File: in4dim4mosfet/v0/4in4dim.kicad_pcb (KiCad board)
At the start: 2 copper layers, 100.1 x 86.4 mm, 89 parts, among them IC1 ATTINY48-A, J1 RJ45, J2 RJ45, J3 CONN_6, K1 CONN_3, P1 CONN_5, P100 CONN_2, P101 CONN_2, P102 CONN_2, P103 CONN_2, P105 CONN_2, P106 CONN_2, P110 CONN_2, P120 CONN_2, P130 CONN_2, P140 CONN_2, P2 CONN_2, P3 CONN_6X2, Q1 SPP20N60C3, Q2 SPP20N60C3, Q3 SPP20N60C3, Q4 SPP20N60C3, U1 7805, U2 LTV847, U3 LTV847

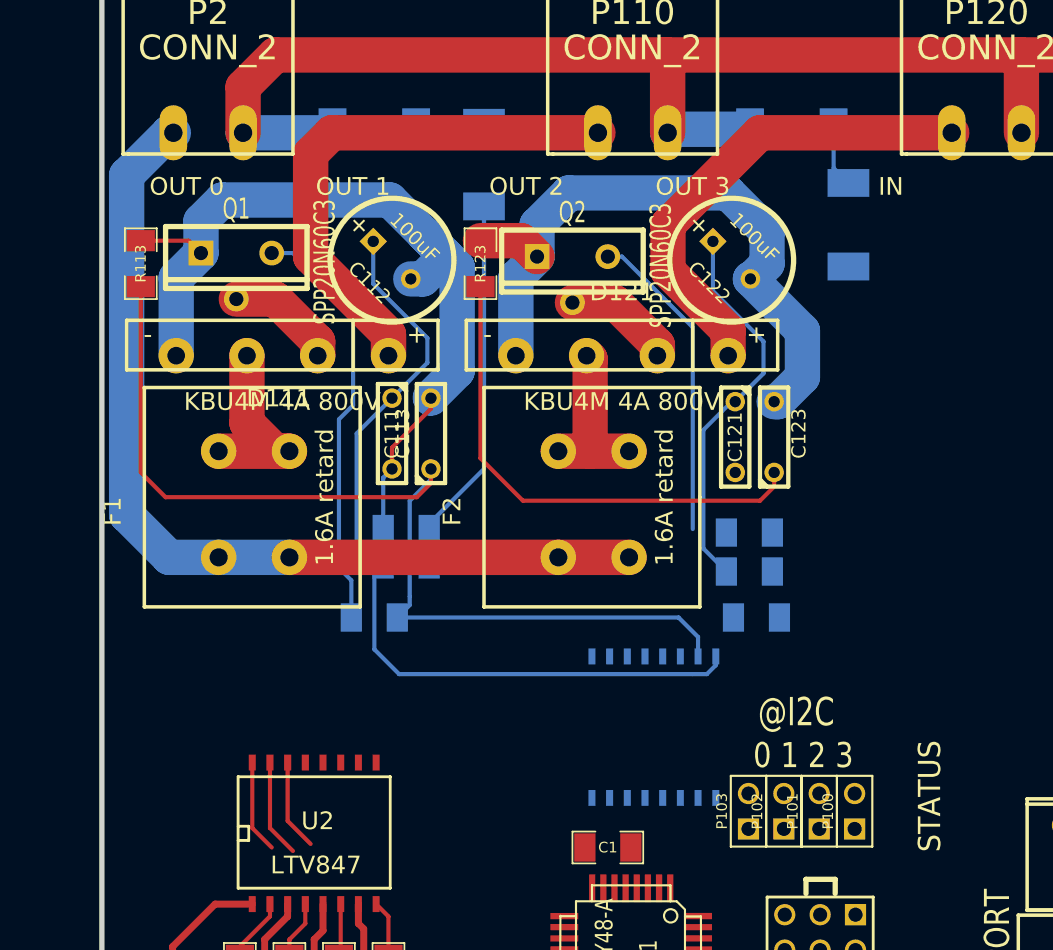
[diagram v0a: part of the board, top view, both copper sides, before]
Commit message: amelioration routage partie puissance pour liberer les deux faces pour le passage de la puissance
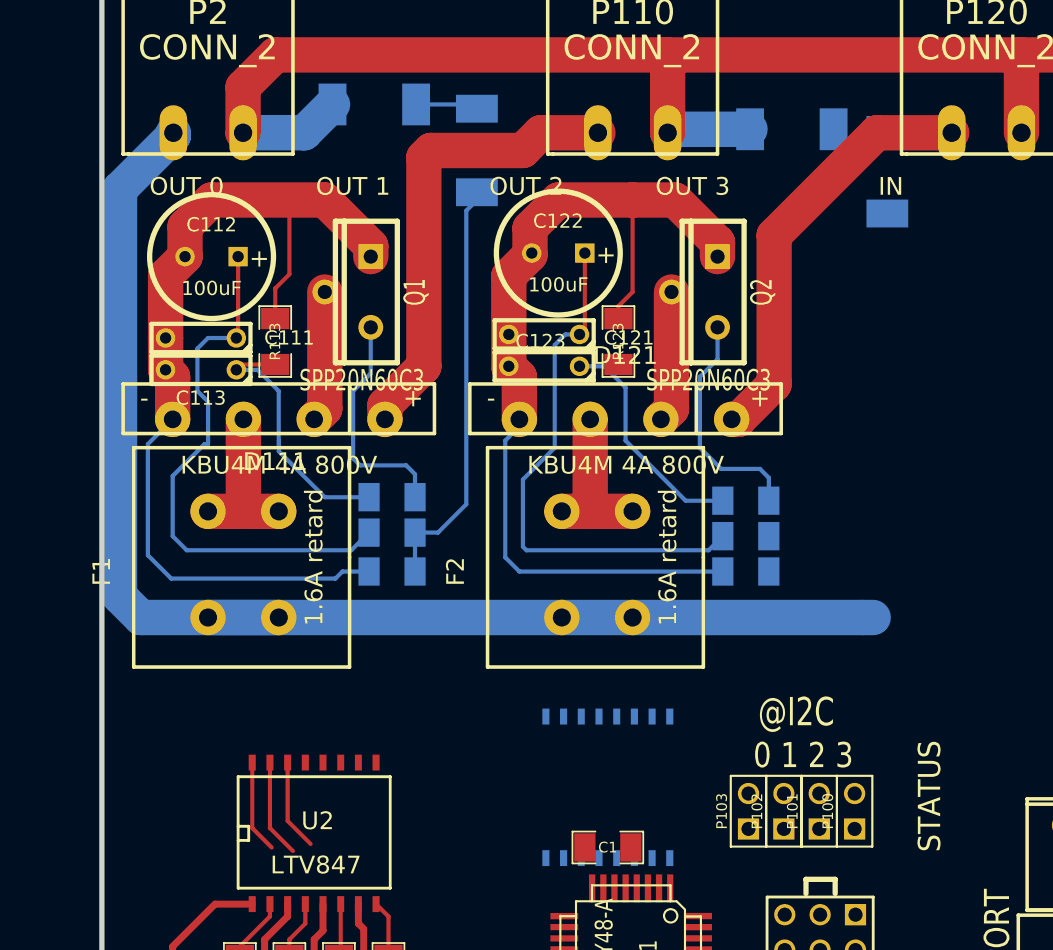
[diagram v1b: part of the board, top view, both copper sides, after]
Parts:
- moved C123 17.3 mm to (213.4, 98.0), turned to 180 degrees
- moved C113 17.1 mm to (188.7, 98.3), turned to 180 degrees
- moved C121 15.6 mm to (213.4, 95.8), turned to 180 degrees
- moved C111 15.3 mm to (188.7, 96.0), turned to 180 degrees
- moved C112 13.0 mm to (189.5, 90.2), turned to 180 degrees
- moved C122 12.5 mm to (214.4, 89.9), turned to 180 degrees
- moved R123 11.4 mm to (218.7, 96.3)
- moved R113 11.2 mm to (194.1, 96.3)
- moved Q2 10.7 mm to (225.8, 92.7), turned to 180 degrees
- moved Q1 10.0 mm to (200.9, 92.7), turned to 180 degrees
- moved R114 8.73 mm to (202.4, 107.4), turned to 180 degrees
- moved R124 8.42 mm to (227.8, 107.7)
- moved U3 5.44 mm to (217.9, 128.3)
- moved R122 4.72 mm to (238.0, 84.1)
- moved D111 4.58 mm to (194.3, 101.9)
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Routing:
- net OUT0_B: track 71.8 -> 18.8 mm
- net /110S: track 63.7 -> 93.0 mm
- net L: track 66.3 -> 94.7 mm
- net OUT0_A: track 60.4 -> 39.0 mm
- net OUT1_B: track 36.1 -> 16.5 mm
- net /120S: track 48.5 -> 66.5 mm
- net N-0000051: track 30.3 -> 16.5 mm
- net OUT1_A: track 27.8 -> 38.4 mm
- net N-0000077: track 22.7 -> 16.7 mm
- net /110P: track 38.0 -> 33.2 mm
- net N-0000082: track 4.30 -> 0.00 mm
- net /120M: track 34.3 -> 30.6 mm
- net /110L: track 13.8 -> 16.7 mm
- net N-0000011: track 27.3 -> 30.0 mm
- net /120D: track 8.12 -> 9.46 mm
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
